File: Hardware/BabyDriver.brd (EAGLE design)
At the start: 73.7 x 49.5 mm, 34 parts, among them U1 L6470

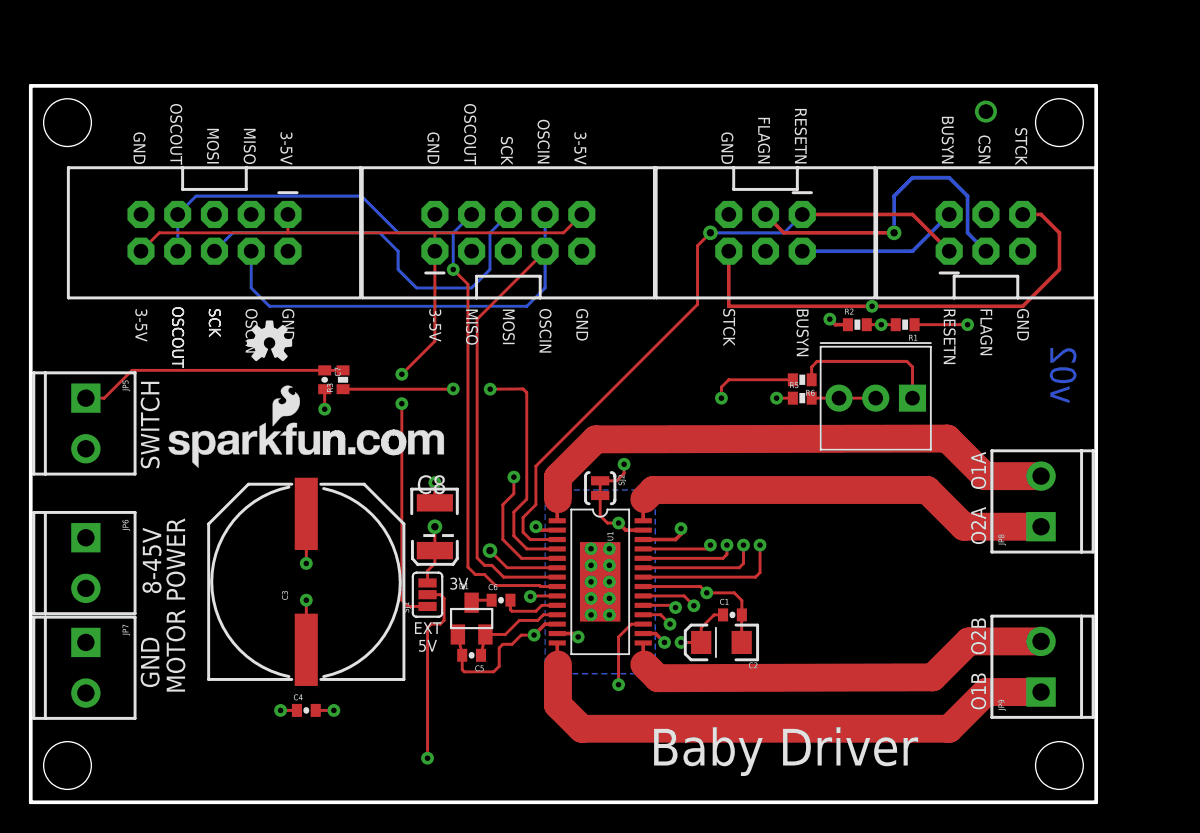
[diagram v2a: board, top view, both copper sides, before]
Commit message: Changes for v02- second proto round Shrank overall board size by about 15% Added a pad for extra chip select signal Improved text placement
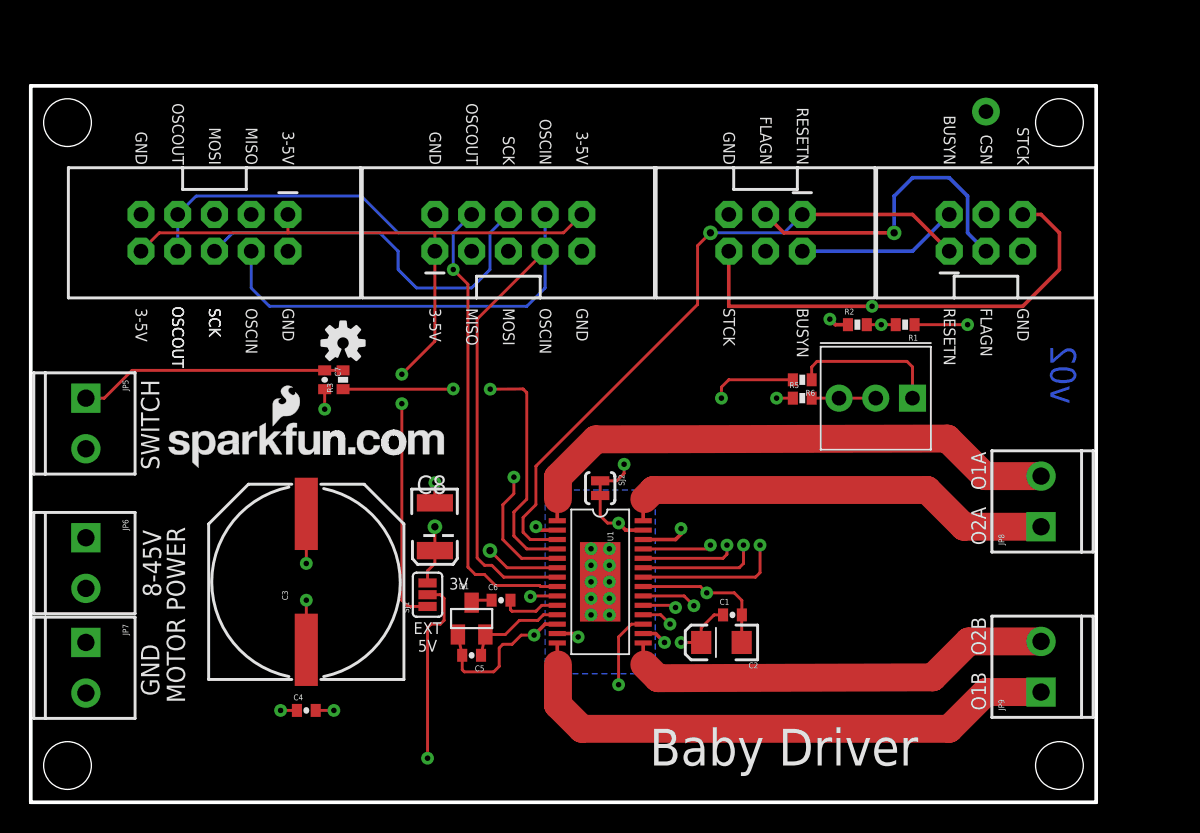
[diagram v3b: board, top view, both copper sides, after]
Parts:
- moved LOGO1 5.08 mm to (21.6, 31.8)
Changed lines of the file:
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@@
 <text x="66.04" y="10.16" size="1.016" layer="21" font="vector" ratio="15" rot="R90">O2B</text>
 <text x="66.04" y="17.78" size="1.016" layer="21" font="vector" ratio="15" rot="R90">O2A</text>
-<text x="7.112" y="44.069" size="0.8128" layer="21" font="vector" ratio="15" rot="SR270" align="bottom-right">GND</text>
+<text x="7.239" y="44.069" size="0.8128" layer="21" font="vector" ratio="15" rot="SR270" align="bottom-right">GND</text>
 <text x="72.263" y="31.623" size="1.778" layer="16" font="vector" ratio="15" rot="MR270">v02</text>
 <wire x1="0" y1="0" x2="73.66" y2="0" width="0.254" layer="20"/>
@@
 <text x="35.179" y="34.163" size="0.8128" layer="21" font="vector" ratio="15" rot="SR270">OSCIN</text>
 <text x="37.719" y="34.163" size="0.8128" layer="21" font="vector" ratio="15" rot="SR270">GND</text>
-<text x="9.652" y="44.069" size="0.8128" layer="21" font="vector" ratio="15" rot="SR270" align="bottom-right">OSCOUT</text>
-<text x="12.192" y="44.069" size="0.8128" layer="21" font="vector" ratio="15" rot="SR270" align="bottom-right">MOSI</text>
-<text x="14.732" y="44.069" size="0.8128" layer="21" font="vector" ratio="15" rot="SR270" align="bottom-right">MISO</text>
-<text x="17.272" y="44.069" size="0.8128" layer="21" font="vector" ratio="15" rot="SR270" align="bottom-right">3-5V</text>
-<text x="27.432" y="44.069" size="0.8128" layer="21" font="vector" ratio="15" rot="SR270" align="bottom-right">GND</text>
-<text x="29.972" y="44.069" size="0.8128" layer="21" font="vector" ratio="15" rot="SR270" align="bottom-right">OSCOUT</text>
-<text x="32.512" y="44.069" size="0.8128" layer="21" font="vector" ratio="15" rot="SR270" align="bottom-right">SCK</text>
-<text x="35.052" y="44.069" size="0.8128" layer="21" font="vector" ratio="15" rot="SR270" align="bottom-right">OSCIN</text>
-<text x="37.592" y="44.069" size="0.8128" layer="21" font="vector" ratio="15" rot="SR270" align="bottom-right">3-5V</text>
-<text x="47.752" y="44.069" size="0.8128" layer="21" font="vector" ratio="15" rot="SR270" align="bottom-right">GND</text>
-<text x="50.292" y="44.069" size="0.8128" layer="21" font="vector" ratio="15" rot="SR270" align="bottom-right">FLAGN</text>
-<text x="52.832" y="44.069" size="0.8128" layer="21" font="vector" ratio="15" rot="SR270" align="bottom-right">RESETN</text>
-<text x="62.992" y="44.069" size="0.8128" layer="21" font="vector" ratio="15" rot="SR270" align="bottom-right">BUSYN</text>
-<text x="65.532" y="44.069" size="0.8128" layer="21" font="vector" ratio="15" rot="SR270" align="bottom-right">CSN</text>
-<text x="68.072" y="44.069" size="0.8128" layer="21" font="vector" ratio="15" rot="SR270" align="bottom-right">STCK</text>
+<text x="9.779" y="44.069" size="0.8128" layer="21" font="vector" ratio="15" rot="SR270" align="bottom-right">OSCOUT</text>
+<text x="12.319" y="44.069" size="0.8128" layer="21" font="vector" ratio="15" rot="SR270" align="bottom-right">MOSI</text>
+<text x="14.859" y="44.069" size="0.8128" layer="21" font="vector" ratio="15" rot="SR270" align="bottom-right">MISO</text>
+<text x="17.399" y="44.069" size="0.8128" layer="21" font="vector" ratio="15" rot="SR270" align="bottom-right">3-5V</text>
+<text x="27.559" y="44.069" size="0.8128" layer="21" font="vector" ratio="15" rot="SR270" align="bottom-right">GND</text>
+<text x="30.099" y="44.069" size="0.8128" layer="21" font="vector" ratio="15" rot="SR270" align="bottom-right">OSCOUT</text>
+<text x="32.639" y="44.069" size="0.8128" layer="21" font="vector" ratio="15" rot="SR270" align="bottom-right">SCK</text>
+<text x="35.179" y="44.069" size="0.8128" layer="21" font="vector" ratio="15" rot="SR270" align="bottom-right">OSCIN</text>
+<text x="37.719" y="44.069" size="0.8128" layer="21" font="vector" ratio="15" rot="SR270" align="bottom-right">3-5V</text>
+<text x="47.879" y="44.069" size="0.8128" layer="21" font="vector" ratio="15" rot="SR270" align="bottom-right">GND</text>
+<text x="50.419" y="44.069" size="0.8128" layer="21" font="vector" ratio="15" rot="SR270" align="bottom-right">FLAGN</text>
+<text x="52.959" y="44.069" size="0.8128" layer="21" font="vector" ratio="15" rot="SR270" align="bottom-right">RESETN</text>
+<text x="63.119" y="44.069" size="0.8128" layer="21" font="vector" ratio="15" rot="SR270" align="bottom-right">BUSYN</text>
+<text x="65.659" y="44.069" size="0.8128" layer="21" font="vector" ratio="15" rot="SR270" align="bottom-right">CSN</text>
+<text x="68.199" y="44.069" size="0.8128" layer="21" font="vector" ratio="15" rot="SR270" align="bottom-right">STCK</text>
 <text x="47.879" y="34.163" size="0.8128" layer="21" font="vector" ratio="15" rot="SR270">STCK</text>
 <text x="52.959" y="34.163" size="0.8128" layer="21" font="vector" ratio="15" rot="SR270">BUSYN</text>
@@
 <text x="8.89" y="22.987" size="1.27" layer="21" font="vector" ratio="15" rot="R90">SWITCH</text>
 <text x="29.591" y="15.113" size="0.8128" layer="21" font="vector" ratio="15" align="center">3V</text>
-<text x="9.017" y="14.351" size="1.27" layer="21" font="vector" ratio="15" rot="R90">8-45V</text>
-<text x="8.89" y="7.874" size="1.27" layer="21" font="vector" ratio="15" rot="R90">GND</text>
-<text x="10.668" y="7.493" size="1.27" layer="21" font="vector" ratio="15" rot="R90">MOTOR POWER</text>
+<text x="9.017" y="16.51" size="1.27" layer="21" font="vector" ratio="15" rot="R90" align="bottom-center">8-45V</text>
+<text x="8.89" y="9.144" size="1.27" layer="21" font="vector" ratio="15" rot="R90" align="bottom-center">GND</text>
+<text x="10.668" y="12.954" size="1.27" layer="21" font="vector" ratio="15" rot="R90" align="bottom-center">MOTOR POWER</text>
 <text x="48.641" y="42.037" size="0.8128" layer="22" font="vector" ratio="15" rot="SMR270" align="bottom-right">GND</text>
 <text x="51.181" y="42.037" size="0.8128" layer="22" font="vector" ratio="15" rot="SMR270" align="bottom-right">FLAGN</text>
@@
 <element name="STANDOFF1" library="SparkFun" package="STAND-OFF" value="STAND-OFF" x="71.12" y="46.99"/>
 <element name="STANDOFF3" library="SparkFun" package="STAND-OFF" value="STAND-OFF" x="2.54" y="2.54"/>
-<element name="LOGO1" library="SparkFun" package="OSHW-LOGO-S" value="OSHW-LOGOS" x="16.51" y="31.75"/>
+<element name="LOGO1" library="SparkFun" package="OSHW-LOGO-S" value="OSHW-LOGOS" x="21.59" y="31.75"/>
 <element name="FRAME1" library="SparkFun-Aesthetics" package="CREATIVE_COMMONS" value="FRAME-LETTER" x="11.43" y="-11.43"/>
 <element name="SJ1" library="SparkFun-Passives" package="SJ_3_PASTE1&amp;2" value="" x="27.432" y="14.351" rot="R90"/>
@@
 <wire x1="65.532" y1="42.291" x2="66.04" y2="41.783" width="0.2032" layer="2"/>
 <wire x1="66.04" y1="41.783" x2="66.04" y2="40.64" width="0.2032" layer="2"/>
-<via x="66.04" y="47.752" extent="1-16" drill="1.016" shape="octagon"/>
+<via x="66.04" y="47.752" extent="1-16" drill="1.016" diameter="1.9304" shape="octagon"/>
 <wire x1="65.532" y1="42.291" x2="65.532" y2="47.244" width="0.254" layer="2"/>
 <wire x1="65.532" y1="47.244" x2="66.04" y2="47.752" width="0.254" layer="2"/>

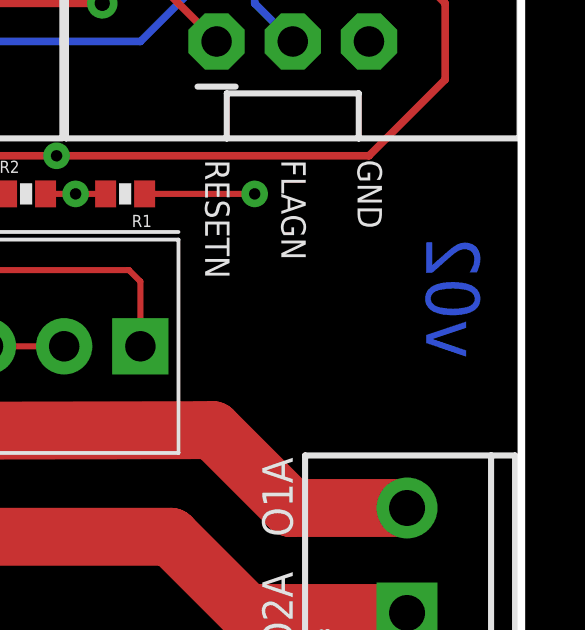
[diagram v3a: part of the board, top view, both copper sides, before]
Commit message: Fix mask on bottom layer
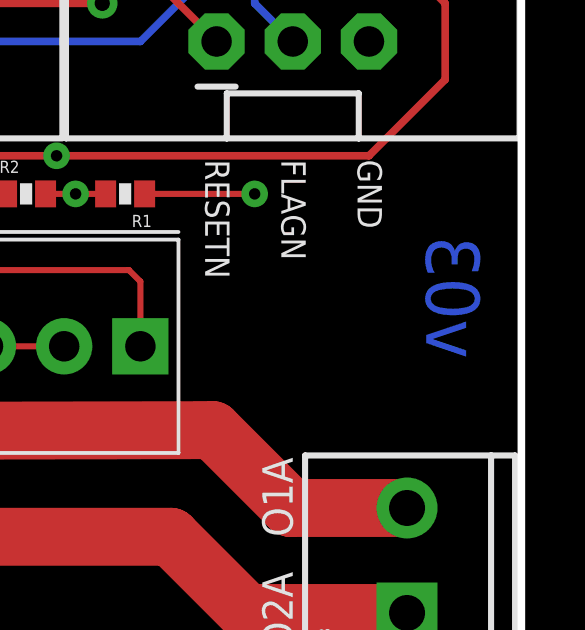
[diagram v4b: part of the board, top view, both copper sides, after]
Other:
- board text added: "v03"
- board text removed: "v02"
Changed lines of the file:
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@@
 <layer number="46" name="Milling" color="3" fill="1" visible="no" active="yes"/>
 <layer number="51" name="tDocu" color="6" fill="1" visible="yes" active="yes"/>
+<layer number="52" name="bDocu" color="7" fill="1" visible="no" active="yes"/>
 <layer number="3" name="Route3" color="4" fill="3" visible="no" active="no"/>
 <layer number="4" name="Route4" color="1" fill="4" visible="no" active="no"/>
@@
 <layer number="49" name="Reference" color="7" fill="1" visible="no" active="no"/>
 <layer number="50" name="dxf" color="7" fill="1" visible="no" active="no"/>
-<layer number="52" name="bDocu" color="7" fill="1" visible="no" active="no"/>
 <layer number="53" name="tGND_GNDA" color="7" fill="9" visible="no" active="no"/>
 <layer number="54" name="bGND_GNDA" color="1" fill="9" visible="no" active="no"/>
@@
 <text x="66.04" y="17.78" size="1.016" layer="21" font="vector" ratio="15" rot="R90">O2A</text>
 <text x="7.239" y="44.069" size="0.8128" layer="21" font="vector" ratio="15" rot="SR270" align="bottom-right">GND</text>
-<text x="72.263" y="31.623" size="1.778" layer="16" font="vector" ratio="15" rot="MR270">v02</text>
+<text x="72.263" y="31.623" size="1.778" layer="16" font="vector" ratio="15" rot="MR270">v03</text>
 <wire x1="0" y1="0" x2="73.66" y2="0" width="0.254" layer="20"/>
 <wire x1="0" y1="0" x2="0" y2="49.53" width="0.254" layer="20"/>

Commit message: Added four-layer warning to files.
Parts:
- added U$4: FOUR_LAYER_WARNING, SparkFun-Aesthetics:FOUR_LAYER_WARNING
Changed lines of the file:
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@@
 <?xml version="1.0" encoding="utf-8"?>
 <!DOCTYPE eagle SYSTEM "eagle.dtd">
-<eagle version="6.3">
+<eagle version="6.4">
 <drawing>
 <settings>
@@
 <element name="JP4" library="SparkFun-Connectors" package="2X3-SHROUDED" value="" x="66.04" y="39.37" rot="R90"/>
 <element name="SJ2" library="SparkFun-Passives" package="SJ_2S-TRACE" value="SOLDERJUMPERTRACE" x="39.37" y="21.717" rot="R270"/>
+<element name="U$4" library="SparkFun-Aesthetics" package="FOUR_LAYER_WARNING" value="FOUR_LAYER_WARNING" x="0" y="-2.54"/>
 </elements>
 <signals>
